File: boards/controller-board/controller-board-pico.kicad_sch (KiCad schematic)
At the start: 71 parts, among them J1 Conn_01x02, J2 Conn_01x02, J3 Conn_01x02, J4 Conn_01x02, J5 Conn_01x03, J6 Phoenix 1995499, Q1 PMV45EN, Q2 Goford_G11S_20V_11A, SW1 EG1271, U1 LTC3624, U2 ADS1015IRUGR, U3 ADS1015IRUGR, U4 RPi_Pico, U5 MCP4728

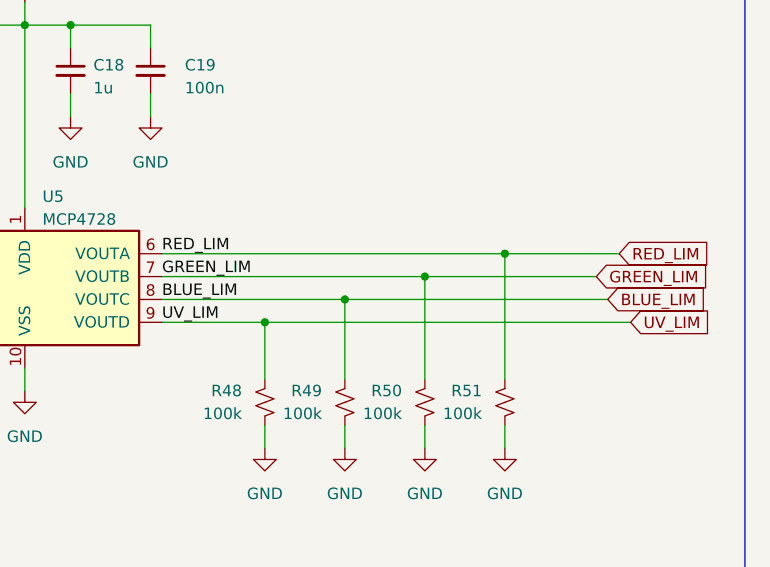
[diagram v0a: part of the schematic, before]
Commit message: completed layout for new LED drivers in schematic
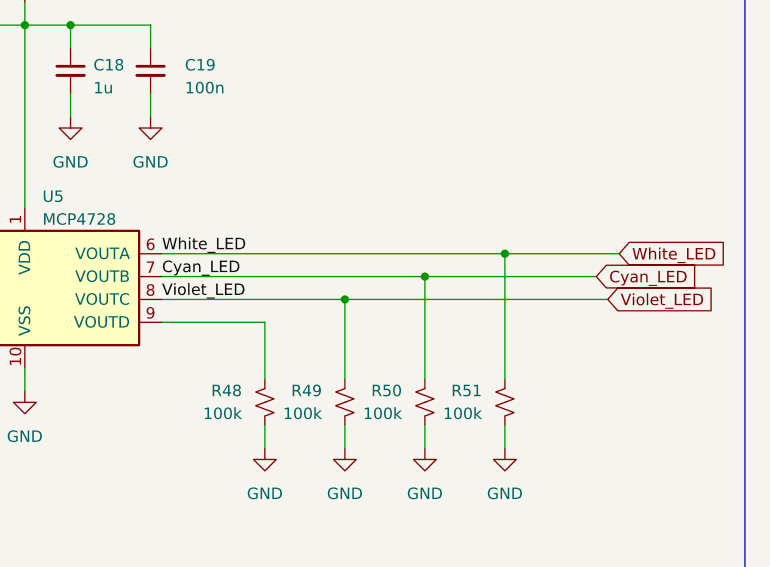
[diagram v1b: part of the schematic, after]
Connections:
- net BLUE_LIM renamed Violet_LED
- net GREEN_LIM renamed Cyan_LED
- net RED_LIM renamed White_LED
- net UV_LIM: no longer names the net of R48.1, U5.9 (VOUTD)
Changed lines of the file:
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@@
-	)
-	(junction
-		(at 368.3 332.74)
-		(diameter 0)
-		(color 0 0 0 0)
 	)
 	(junction
@@
 	(wire
 		(pts
-			(xy 368.3 332.74) (xy 408.94 332.74)
-		)
-		(stroke
-			(width 0)
-			(type default)
-		)
-	)
-	(wire
-		(pts
 			(xy 261.62 332.74) (xy 261.62 208.28)
 		)
@@
 		)
 	)
-	(label "RED_LIM"
+	(label "White_LED"
 		(at 356.87 325.12 0)
 		(fields_autoplaced yes)
@@
 		)
 	)
-	(label "UV_LIM"
-		(at 356.87 332.74 0)
-		(fields_autoplaced yes)
-		(effects
-			(font
-				(size 1.27 1.27)
-			)
-			(justify left bottom)
-		)
-	)
-	(label "GREEN_LIM"
+	(label "Cyan_LED"
 		(at 356.87 327.66 0)
 		(fields_autoplaced yes)
@@
 		)
 	)
-	(label "BLUE_LIM"
+	(label "Violet_LED"
 		(at 356.87 330.2 0)
 		(fields_autoplaced yes)
@@
 		)
 	)
-	(global_label "GREEN_LIM"
+	(global_label "Cyan_LED"
 		(shape input)
 		(at 405.13 327.66 0)
@@
 		)
 		(property "Intersheetrefs" "${INTERSHEET_REFS}"
-			(at 418.3356 327.66 0)
+			(at 417.0655 327.66 0)
 			(effects
 				(font
@@
 		)
 	)
-	(global_label "BLUE_LIM"
+	(global_label "Violet_LED"
 		(shape input)
 		(at 406.4 330.2 0)
@@
 		)
 		(property "Intersheetrefs" "${INTERSHEET_REFS}"
-			(at 418.2147 330.2 0)
+			(at 419.1218 330.2 0)
 			(effects
 				(font
@@
 		)
 	)
-	(global_label "UV_LIM"
+	(global_label "White_LED"
 		(shape input)
-		(at 408.94 332.74 0)
+		(at 407.67 325.12 0)
 		(fields_autoplaced yes)
 		(effects
@@
 		)
 		(property "Intersheetrefs" "${INTERSHEET_REFS}"
-			(at 418.3962 332.74 0)
+			(at 420.0894 325.12 0)
 			(effects
 				(font
-					(size 1.27 1.27)
-				)
-				(justify left)
-				(hide yes)
-			)
-		)
-	)
-	(global_label "RED_LIM"
-		(shape input)
-		(at 407.67 325.12 0)
-		(fields_autoplaced yes)
-		(effects
-			(font
-				(size 1.27 1.27)
-			)
-			(justify left)
-		)
-		(property "Intersheetrefs" "${INTERSHEET_REFS}"
-			(at 418.3961 325.12 0)
-			(effects
-				(font

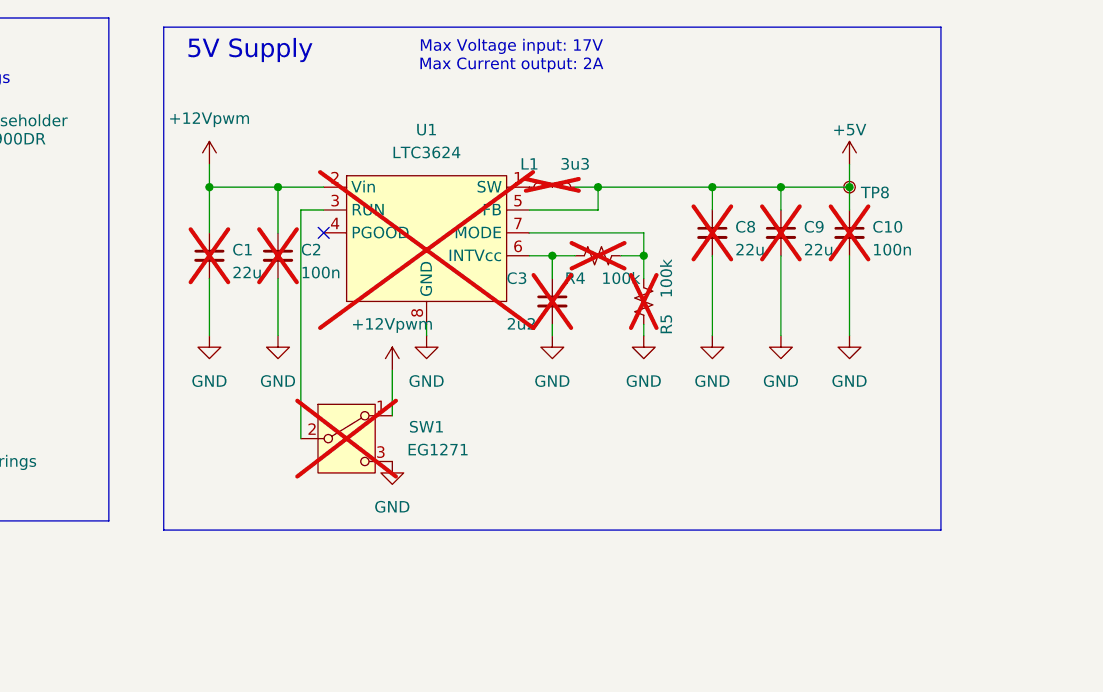
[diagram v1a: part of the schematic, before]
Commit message: grouped components for pcb layout, started routing
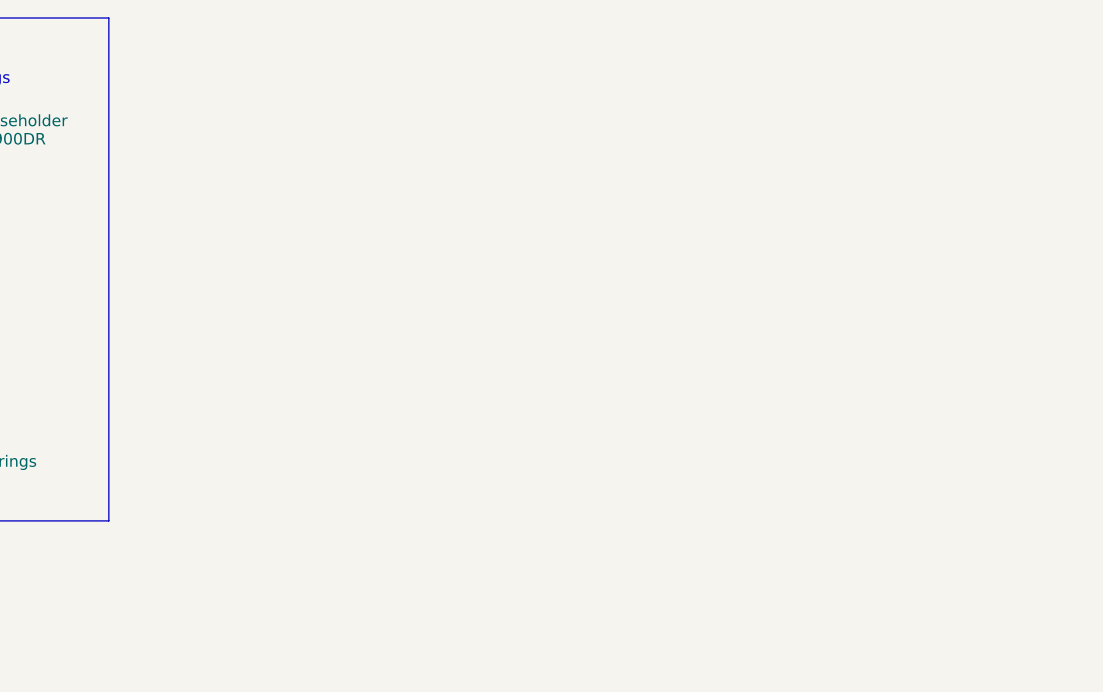
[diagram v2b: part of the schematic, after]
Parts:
- removed C1, C8, C9: 22u, Capacitor_SMD:C_1210_3225Metric, symbol Device:C_Small
- removed C10, C2: 100n, oresat-passives:0603-C-NOSILK, symbol Device:C_Small
- removed C3: 2u2, oresat-passives:0603-C-NOSILK, symbol Device:C_Small
- removed L1: 3u3, oresat-passives:L_ECS-MPI4040, symbol Device:L_Small
- removed R4, R5: 100k, oresat-passives:0603-C-NOSILK, symbol Device:R_Small_US
- removed SW1: EG1271, Button_Switch_THT:SW_E-Switch_EG1271_SPDT, symbol Switch:SW_SPDT
- removed TP8: TestPoint-MinTH, oresat-misc:TestPoint-MinTH, symbol oresat-misc:TestPoint-MinTH
- removed U1: LTC3624, oresat-ics:DFN-8-1EP_3x3mm_P0.5mm_EP1.65x2.38mm_ThermalVias0.3mm, symbol oresat-ics:LTC3624
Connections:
- no-connect marks 30 -> 29
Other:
- note removed: "5V Supply"
- note removed: "Max Voltage input: 17V Max Current output: 2A"

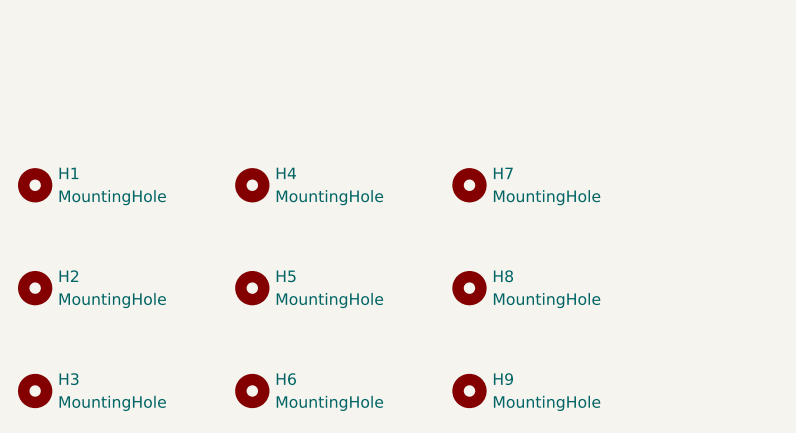
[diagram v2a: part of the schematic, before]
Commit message: updated pcb layout: LED drivers
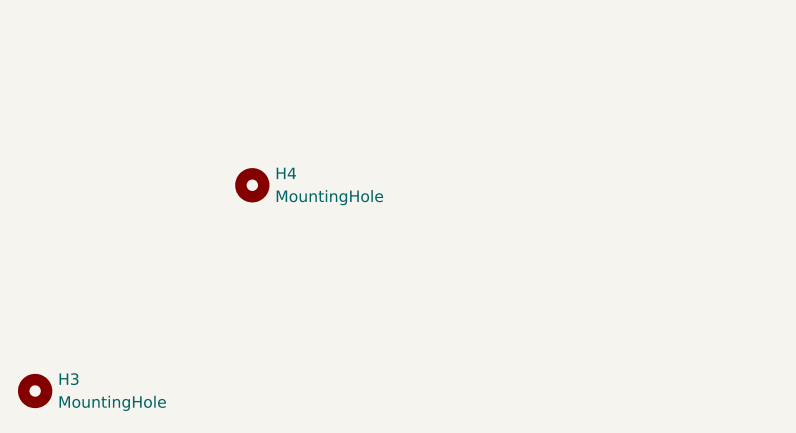
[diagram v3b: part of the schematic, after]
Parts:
- removed H1, H2, H5, H6, H7, H8, H9: MountingHole, oresat-misc:MountingHole_3.2mm_M3, symbol Mechanical:MountingHole
- U4: footprint oresat-misc:RPi_Pico_TH -> oresat-misc:Raspberry Pi Pico Castellated

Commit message: v2 layout. Finally found a way to route the boards with a hopefully decent heatsink. To do: route the other side of the board, add the heatsink to the BOM.
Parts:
- removed C16, C5: 1u, oresat-passives:0603-C-NOSILK, symbol Device:C_Small
- removed C6, C7: 100n, oresat-passives:0603-C-NOSILK, symbol Device:C_Small
- removed H3, H4: MountingHole, oresat-misc:MountingHole_3.2mm_M3, symbol Mechanical:MountingHole
- removed TP4, TP5, TP6, TP7: TestPoint-MinTH, oresat-misc:TestPoint-MinTH, symbol oresat-misc:TestPoint-MinTH
- removed U3: ADS1015IRUGR, Package_DFN_QFN:Texas_R-PUQFN-N10, symbol Analog_ADC:ADS1015IDGS
- added D19: MBR0530, Diode_SMD:D_SOD-123, symbol Diode:MBR0530
- added HW1, HW2, HW3, HW4, HW5, HW6: M2-Press-Fit-Nut, oresat-misc:M2-Press-Fit-Nut, symbol oresat-misc:M2-Press-Fit-Nut
- added R4: 100, oresat-passives:0603-C-NOSILK, symbol Device:R_Small_US
- C15: value 22u -> 22u/25V
- C17: value C_Small -> NP
- J1: value Conn_01x02 -> Phoenix 1935161
- R13: value 0 -> 100; DPN 311-0.0GRCT-ND -> 311-100GRCT-ND; MPN RC0603JR-070RL -> RC0603JR-07100RL
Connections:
- net +12V: now also F2.1; no longer F2.2
- net +12Vpwm: now also F1.1; no longer F1.2
- net GND: now also J1.2 (Pin_2), J6.2 (Pin_2), D19.2 (A); no longer J1.1 (Pin_1), J6.1 (Pin_1)
- net PWM: now also R4.2; no longer U4.34 (GPIO28_ADC2)
- net at Q2.5, Q2.6, Q2.7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: now also J6.1 (Pin_1), D19.1 (K); no longer J6.2 (Pin_2)
- new net: F1.2, F2.2, J1.1 (Pin_1), TP1.1
- new net: R4.1, U4.34 (GPIO28_ADC2)
- no-connect marks 29 -> 28
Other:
- note added: "(out)"
- note added: "1210"
- note added: "3D printed sheet metal adapter mounting holes"
- note added: "Mounting holes for Halogen"
- note added: "TBD: R13/C17 may need to be stuffed with something to slow down Q2 rise time to prevent ringing and overshoot and whatnot."
- note removed: "Input from SS if stuffed"
- note removed: "Output to SS"
- note removed: "TBD: R13 may need to be stuffed with something to slow down Q2 rise time to prevent ringing and overshoot and whatnot."
- moved on the sheet: C15, C17, J1, J6, R13
